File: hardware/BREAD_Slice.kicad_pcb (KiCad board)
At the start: 2 copper layers, 72.6 x 100 mm, 16 parts, among them J1 Conn_01x10_Female, J2 I2C_01x04

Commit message: Initial commit
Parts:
- removed C4: 22uF, Capacitor_SMD:C_1206_3216Metric
- removed HS1: Heatsink_Pad, SparkFun-Fuse:Thermal Pad
- removed U1: ~, Package_TO_SOT_SMD:TSOT-23-6
- added J3: Term_2, OCI_UPL_FOOTPRINTS:TerminalBlock_Pheonix_MKDS1.5-2pol, F.Cu at (184.8, 53.4)
- added Q1: TIP120, OCI_UPL_FOOTPRINTS:TO-220_Neutral123_Vertical_LargePads, F.Cu at (144.2, 82.7)
- added R1: 100k, Resistor_THT:R_Axial_DIN0309_L9.0mm_D3.2mm_P15.24mm_Horizontal, F.Cu at (165.8, 59.8)
- added RV1: 100k, Potentiometer_THT:Potentiometer_Bourns_3266W_Vertical, F.Cu at (159.9, 87.1)
- C1: value 22uF -> 10uF_t; footprint Capacitor_SMD:C_1206_3216Metric -> OCI_UPL_FOOTPRINTS:C_2312
- C2: value 100nF -> 10uF_t; footprint Capacitor_SMD:C_1206_3216Metric -> OCI_UPL_FOOTPRINTS:C_2312
- C3: value 22uF -> 100uF; footprint Capacitor_SMD:C_1206_3216Metric -> OCI_UPL_FOOTPRINTS:C_Radial_D8_L11.5_P3.5; moved to F.Cu
- D1: value WS2812B_5050 -> D; footprint SparkFun-LED:WS2812-5050-4PIN -> OCI_UPL_FOOTPRINTS:Diode_DO-41_SOD81_Horizontal_RM10
- H1, H4: footprint MountingHole:MountingHole_5mm -> MountingHole:MountingHole_3.2mm_M3_DIN965_Pad
- H2: renamed from H3; footprint MountingHole:MountingHole_5mm -> MountingHole:MountingHole_3.2mm_M3_DIN965_Pad
- H3: renamed from H2; footprint MountingHole:MountingHole_5mm -> MountingHole:MountingHole_3.2mm_M3_DIN965_Pad
- J2: value I2C_01x04 -> Term_2; footprint Connector_JST:JST_SH_SM04B-SRSS-TB_1x04-1MP_P1.00mm_Horizontal -> OCI_UPL_FOOTPRINTS:TerminalBlock_Pheonix_MKDS1.5-2pol; moved to F.Cu
- L1: value 4.7uH -> 560 uH; footprint Inductor_SMD:L_1210_3225Metric -> Inductor_THT:L_Radial_D28.0mm_P29.20mm; moved to F.Cu
- moved Logo1 78.8 mm to (174.7, 134.7), turned to 0 degrees
- moved C3 77.3 mm to (169.6, 50.9)
- moved D1 69.8 mm to (135.3, 77.6), turned to -90 degrees
- moved J2 68.3 mm to (184.8, 77.6), turned to -90 degrees
- moved L1 63.0 mm to (131.5, 59.8)
- moved C1 35.5 mm to (157.6, 99.0), turned to 0 degrees
- moved C2 32.3 mm to (157.6, 107.8), turned to 0 degrees
- moved A1 7.59 mm to (135.0, 100.0)
- moved J1 3.43 mm to (129.6, 78.8)
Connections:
- A1 pad 1: unconnected-(A1-D1/TX-Pad1) -> Net-(A1-Pad1)
- A1 pad 10: unconnected-(A1-D7-Pad10) -> Net-(A1-Pad10)
- A1 pad 11: unconnected-(A1-D8-Pad11) -> Net-(A1-Pad11)
- A1 pad 12: unconnected-(A1-D9-Pad12) -> Net-(A1-Pad12)
- A1 pad 13: unconnected-(A1-D10-Pad13) -> Net-(A1-Pad13)
- A1 pad 14: unconnected-(A1-D11-Pad14) -> Net-(A1-Pad14)
- A1 pad 15: unconnected-(A1-D12-Pad15) -> Net-(A1-Pad15)
- A1 pad 16: unconnected-(A1-D13-Pad16) -> Net-(A1-Pad16)
- A1 pad 17: unconnected-(A1-3V3-Pad17) -> Net-(A1-Pad17)
- A1 pad 18: unconnected-(A1-AREF-Pad18) -> Net-(A1-Pad18)
- A1 pad 19: unconnected-(A1-A0-Pad19) -> /FB
- A1 pad 2: unconnected-(A1-D0/RX-Pad2) -> Net-(A1-Pad2)
- A1 pad 20: unconnected-(A1-A1-Pad20) -> Net-(A1-Pad20)
- A1 pad 21: unconnected-(A1-A2-Pad21) -> Net-(A1-Pad21)
- A1 pad 22: unconnected-(A1-A3-Pad22) -> Net-(A1-Pad22)
- A1 pad 25: unconnected-(A1-A6-Pad25) -> Net-(A1-Pad25)
- A1 pad 26: unconnected-(A1-A7-Pad26) -> Net-(A1-Pad26)
- A1 pad 28: unconnected-(A1-~{RESET}-Pad28) -> Net-(A1-Pad28)
- A1 pad 3: unconnected-(A1-~{RESET}-Pad3) -> Net-(A1-Pad3)
- A1 pad 30: unconnected-(A1-VIN-Pad30) -> +12V
- A1 pad 8: /LED -> Net-(A1-Pad8)
- A1 pad 9: unconnected-(A1-D6-Pad9) -> /SW
- C1 pad 1: GND -> +12V
- C1 pad 2: +12V -> GND
- C2 pad 1: Net-(U1-SW) -> +5V
- C2 pad 2: Net-(U1-BST) -> GND
- C3 pad 1: GND -> Net-(C3-Pad1)
- C3 pad 2: +5V -> GND
- D1 pad 1: +5V -> Net-(D1-Pad1)
- D1 pad 2: unconnected-(D1-DOUT-Pad2) -> GND
- J2 pad 2: +5V -> Net-(J2-Pad2)
- L1 pad 1: Net-(U1-SW) -> Net-(D1-Pad1)
- L1 pad 2: +5V -> Net-(C3-Pad1)
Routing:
- net /FB: track 0.00 -> 117.8 mm
- net +5V: track 108.9 -> 4.86 mm, vias 1 -> 0
- net /LED: track 51.5 -> 0.00 mm
- net Net-(J2-Pad2): track 0.00 -> 45.7 mm
- net /SW: track 0.00 -> 42.5 mm
- net Net-(D1-Pad1): track 0.00 -> 30.8 mm
- net Net-(C3-Pad1): track 0.00 -> 30.4 mm
- net +12V: track 46.8 -> 75.7 mm, vias 0 -> 2
- net GND: track 19.6 -> 0.00 mm, vias 14 -> 0
- net /I2C_CLK: track 78.5 -> 69.3 mm
- net /I2C_DAT: track 76.6 -> 85.6 mm
- net /E_STOP: track 30.1 -> 22.0 mm
- net /INT: track 28.8 -> 22.0 mm
- net /SYNC: track 27.9 -> 21.2 mm
- net Net-(U1-SW): track 5.22 -> 0.00 mm
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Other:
- board size 72.6 x 100 mm -> 70 x 100 mm
- board text added: "+"
- board text added: "Buck Converter Slice SLC_BUCK R0 2021"
- board text added: "V in"
- board text added: "V out"
- board text removed: "12V"
- board text removed: "12V->5V Reg"
- board text removed: "5V I2C Connector"
- board text removed: "ARDUINO NANO"
- board text removed: "BREAD Slice Template SLC_TEMP <version> <year>"
- board text removed: "ESTOP"
- board text removed: "INT"
- board text removed: "LED"
- board text removed: "SCL"
- board text removed: "SDA"
- board text removed: "SYNC"

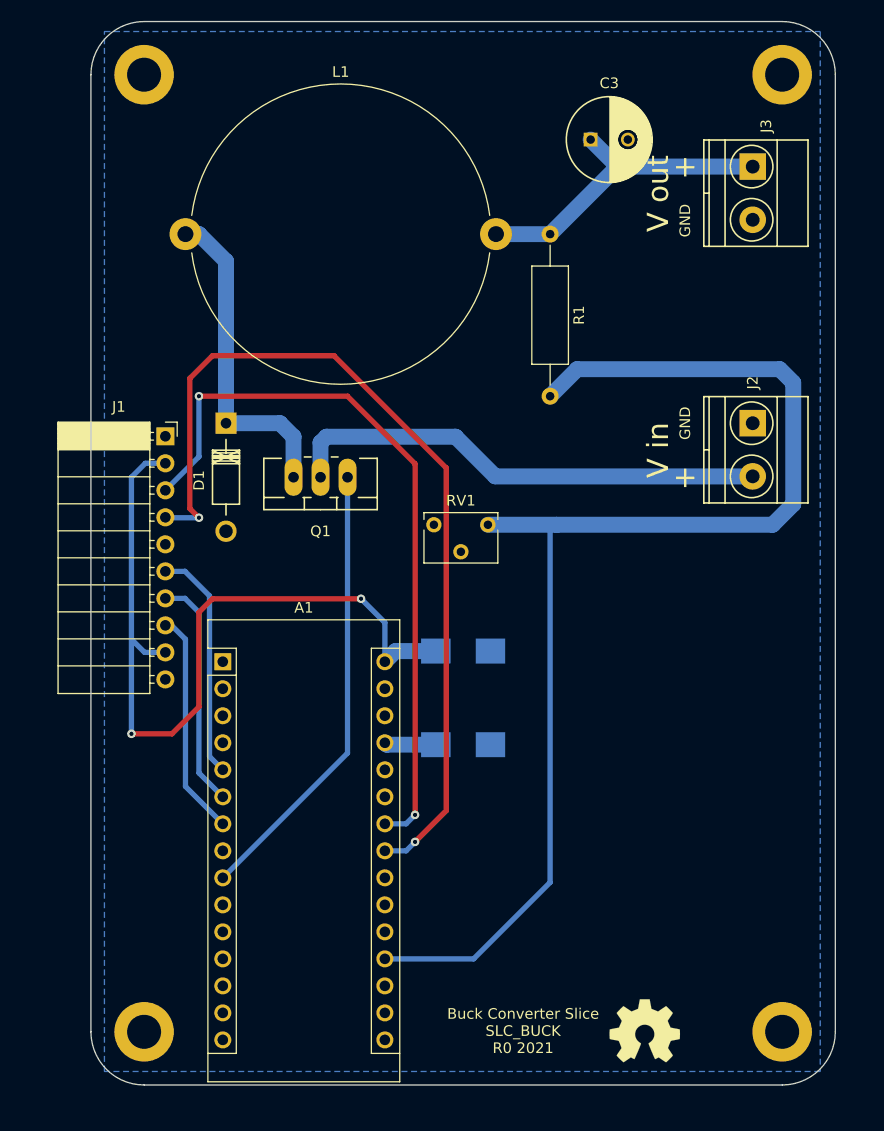
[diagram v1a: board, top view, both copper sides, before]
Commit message: updated to new BREAD format
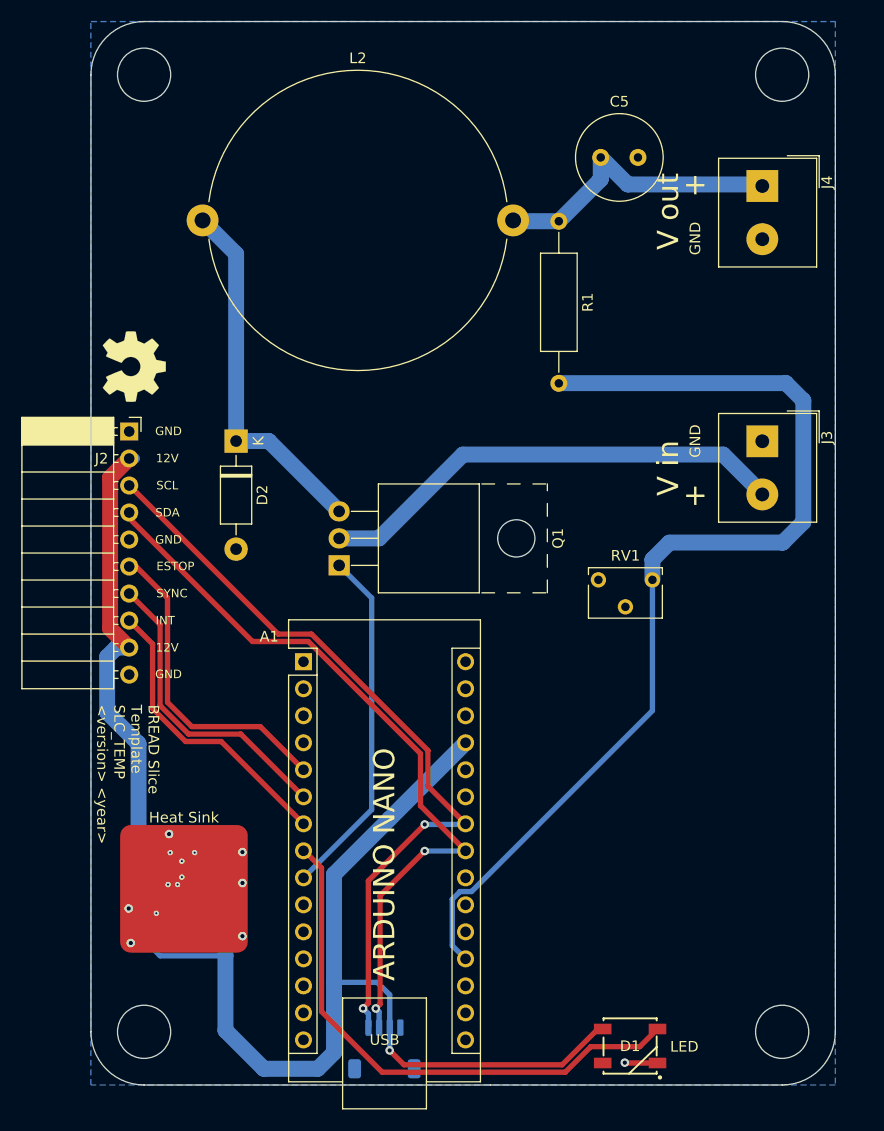
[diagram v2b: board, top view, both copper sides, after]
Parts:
- removed the J2 at (184.8, 77.6)
- added C4: 22uF, Capacitor_SMD:C_1206_3216Metric, B.Cu at (133.8, 116.5)
- added C5: 100uF, Capacitor_THT:C_Radial_D8.0mm_H11.5mm_P3.50mm, F.Cu at (170.5, 52.6)
- added D2: D, Diode_THT:D_DO-41_SOD81_P10.16mm_Horizontal, F.Cu at (136.2, 79.2)
- added HS1: Heatsink_Pad, KML-Custom:Thermal Pad, F.Cu at (131.3, 121.4)
- added J1: I2C_01x04, Connector_JST:JST_SH_SM04B-SRSS-TB_1x04-1MP_P1.00mm_Horizontal, B.Cu at (150.2, 136.4)
- added J4: Term_2, TerminalBlock_Altech:Altech_AK100_1x02_P5.00mm, F.Cu at (185.7, 55.3)
- added L2: 560 uH, Inductor_THT:L_Radial_D28.0mm_P29.20mm, F.Cu at (133.1, 58.5)
- added U1: ~, Package_TO_SOT_SMD:TSOT-23-6, B.Cu at (128.8, 122.8)
- C1: value 10uF_t -> 22uF; footprint OCI_UPL_FOOTPRINTS:C_2312 -> Capacitor_SMD:C_1206_3216Metric
- C2: value 10uF_t -> 100nF; footprint OCI_UPL_FOOTPRINTS:C_2312 -> Capacitor_SMD:C_1206_3216Metric
- C3: value 100uF -> 22uF; footprint OCI_UPL_FOOTPRINTS:C_Radial_D8_L11.5_P3.5 -> Capacitor_SMD:C_1206_3216Metric; moved to B.Cu
- D1: value D -> WS2812B_5050; footprint OCI_UPL_FOOTPRINTS:Diode_DO-41_SOD81_Horizontal_RM10 -> SparkFun-LED:WS2812-5050-4PIN
- H1, H4: footprint MountingHole:MountingHole_3.2mm_M3_DIN965_Pad -> MountingHole:MountingHole_5mm
- H2: renamed from H3; footprint MountingHole:MountingHole_3.2mm_M3_DIN965_Pad -> MountingHole:MountingHole_5mm
- H3: renamed from H2; footprint MountingHole:MountingHole_3.2mm_M3_DIN965_Pad -> MountingHole:MountingHole_5mm
- J3: footprint OCI_UPL_FOOTPRINTS:TerminalBlock_Pheonix_MKDS1.5-2pol -> TerminalBlock_Altech:Altech_AK100_1x02_P5.00mm
- L1: value 560 uH -> 4.7uH; footprint Inductor_THT:L_Radial_D28.0mm_P29.20mm -> Inductor_SMD:L_1210_3225Metric; moved to B.Cu
- Q1: footprint OCI_UPL_FOOTPRINTS:TO-220_Neutral123_Vertical_LargePads -> Package_TO_SOT_THT:TO-220-3_Horizontal_TabUp
- moved Logo1 78.8 mm to (126.7, 72.2), turned to -90 degrees
- moved C3 77.3 mm to (133.8, 119.5)
- moved D1 69.8 mm to (173.3, 136.1), turned to 0 degrees
- moved L1 63.0 mm to (133.8, 122.8)
- moved C1 35.5 mm to (128.6, 119.5), turned to 180 degrees
- moved C2 32.3 mm to (131.2, 126.3), turned to 180 degrees
- moved J3 25.8 mm to (185.7, 79.3)
- moved RV1 16.3 mm to (175.4, 92.3)
- moved Q1 8.47 mm to (145.9, 90.9), turned to 90 degrees
- moved A1 7.59 mm to (142.6, 100.0)
- moved J2 3.43 mm to (126.2, 78.3)
- moved R1 1.46 mm to (166.6, 58.6)
- renumbered J1 to J2
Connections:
- net /FB renamed /feedback
- net /SW renamed /switching
- A1 pad 1: Net-(A1-Pad1) -> unconnected-(A1-D1/TX-Pad1)
- A1 pad 10: Net-(A1-Pad10) -> unconnected-(A1-D7-Pad10)
- A1 pad 11: Net-(A1-Pad11) -> unconnected-(A1-D8-Pad11)
- A1 pad 12: Net-(A1-Pad12) -> unconnected-(A1-D9-Pad12)
- A1 pad 13: Net-(A1-Pad13) -> unconnected-(A1-D10-Pad13)
- A1 pad 14: Net-(A1-Pad14) -> unconnected-(A1-D11-Pad14)
- A1 pad 15: Net-(A1-Pad15) -> unconnected-(A1-D12-Pad15)
- A1 pad 16: Net-(A1-Pad16) -> unconnected-(A1-D13-Pad16)
- A1 pad 17: Net-(A1-Pad17) -> unconnected-(A1-3V3-Pad17)
- A1 pad 18: Net-(A1-Pad18) -> unconnected-(A1-AREF-Pad18)
- A1 pad 2: Net-(A1-Pad2) -> unconnected-(A1-D0/RX-Pad2)
- A1 pad 20: Net-(A1-Pad20) -> unconnected-(A1-A1-Pad20)
- A1 pad 21: Net-(A1-Pad21) -> unconnected-(A1-A2-Pad21)
- A1 pad 22: Net-(A1-Pad22) -> unconnected-(A1-A3-Pad22)
- A1 pad 25: Net-(A1-Pad25) -> unconnected-(A1-A6-Pad25)
- A1 pad 26: Net-(A1-Pad26) -> unconnected-(A1-A7-Pad26)
- A1 pad 28: Net-(A1-Pad28) -> unconnected-(A1-~{RESET}-Pad28)
- A1 pad 3: Net-(A1-Pad3) -> unconnected-(A1-~{RESET}-Pad3)
- A1 pad 30: +12V -> unconnected-(A1-VIN-Pad30)
- A1 pad 8: Net-(A1-Pad8) -> /LED
- C1 pad 1: +12V -> GND
- C1 pad 2: GND -> +12V
- C2 pad 1: +5V -> Net-(U1-SW)
- C2 pad 2: GND -> Net-(U1-BST)
- C3 pad 1: Net-(C3-Pad1) -> GND
- C3 pad 2: GND -> +5V
- D1 pad 1: Net-(D1-Pad1) -> +5V
- D1 pad 2: GND -> unconnected-(D1-DOUT-Pad2)
- J3 pad 1: Net-(C3-Pad1) -> GND
- J3 pad 2: GND -> Net-(Q1-C)
- L1 pad 1: Net-(D1-Pad1) -> Net-(U1-SW)
- L1 pad 2: Net-(C3-Pad1) -> +5V
- Q1 pad 2: Net-(J2-Pad2) -> Net-(Q1-C)
- Q1 pad 3: Net-(D1-Pad1) -> Net-(D2-K)
- R1 pad 1: Net-(C3-Pad1) -> Net-(C5-Pad1)
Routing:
- net +5V: track 4.86 -> 108.9 mm, vias 0 -> 1
- net /LED: track 0.00 -> 51.5 mm
- net Net-(J2-Pad2): track 45.7 -> 0.00 mm
- net Net-(Q1-C): track 0.00 -> 44.6 mm
- net Net-(D2-K): track 0.00 -> 34.5 mm
- net Net-(D1-Pad1): track 30.8 -> 0.00 mm
- net Net-(C3-Pad1): track 30.4 -> 0.00 mm
- net +12V: track 75.7 -> 46.8 mm, vias 2 -> 0
- net Net-(C5-Pad1): track 0.00 -> 28.3 mm
- net /feedback: track 117.8 -> 97.2 mm
- net GND: track 0.00 -> 19.6 mm, vias 0 -> 14
- net /I2C_DAT: track 85.6 -> 70.5 mm
- net /switching: track 42.5 -> 33.3 mm
- net /E_STOP: track 22.0 -> 30.1 mm
- net /INT: track 22.0 -> 28.8 mm
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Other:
- outline, holes or cut-outs redrawn
- board text added: "12V"
- board text added: "12V->5V Reg"
- board text added: "5V I2C Connector"
- board text added: "ARDUINO NANO"
- board text added: "BREAD Slice Template SLC_TEMP <version> <year>"
- board text added: "ESTOP"
- board text added: "INT"
- board text added: "LED"
- board text added: "SCL"
- board text added: "SDA"
- board text added: "SYNC"
- board text removed: "Buck Converter Slice SLC_BUCK R0 2021"
